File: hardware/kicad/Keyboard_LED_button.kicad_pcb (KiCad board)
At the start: 2 copper layers, 20 x 20 mm, 27 parts, among them J1 JST 4 Pin Qwiic I2C Connector, J2 JST 4 Pin Qwiic I2C Connector, J3 Castellated_Edge_4pin_Qwiic_S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, J4 Castellated_Edge_5pin_Firmware, SW1 SW_Push, U1 CH32V003F4U6, U2 MT3540‑F23

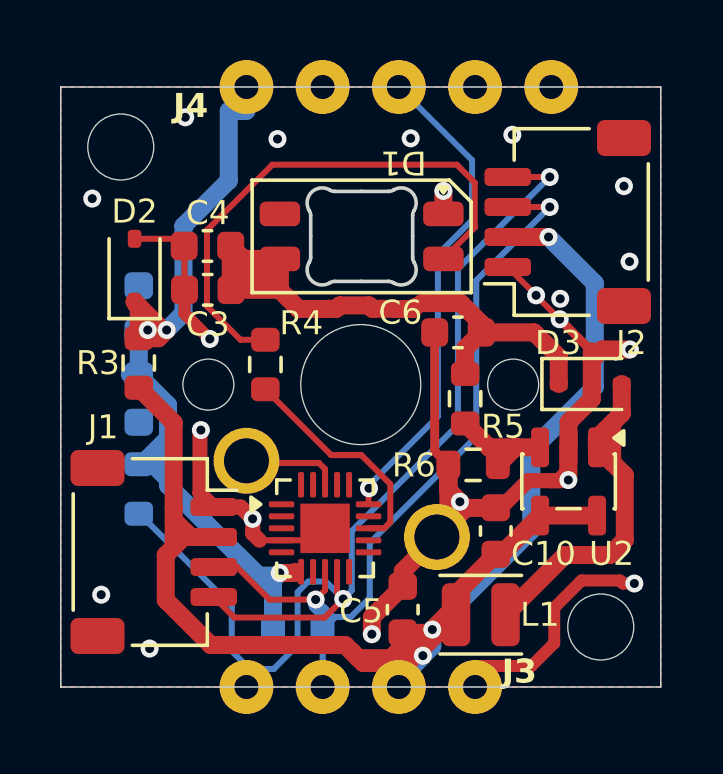
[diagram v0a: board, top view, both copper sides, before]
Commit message: LED Button V2 hardware: updated KiCad schematic + PCB; add V2 + V1.1 schematic PDFs
Updated Keyboard_LED_button KiCad project (schematic + board) for v2.0; added
Schematics_LEDButton_V2_20260616.pdf and renamed-as Schematics_LEDButton_V1_1_20260408.pdf;
removed obsolete Schematics_Keyboard_Button_20260408.pdf and .keep placeholders.
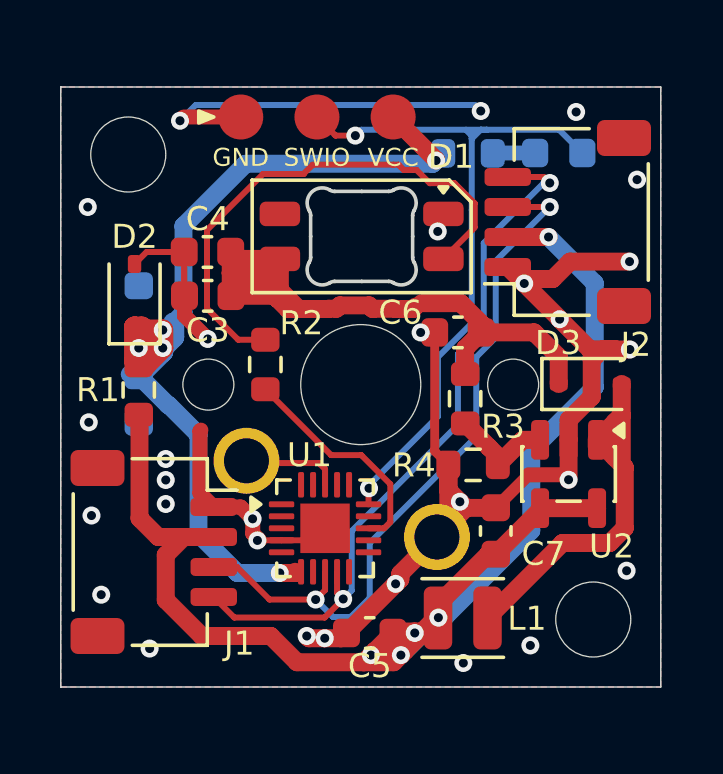
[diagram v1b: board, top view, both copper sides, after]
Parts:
- removed H2: MountingHole, MountingHole:MountingHole_2.2mm_M2
- removed J4: Castellated_Edge_5pin_Firmware, Chris_Library:Castellated_edge_pad_Firmware
- removed the R1 at (122.6, 93.4)
- removed the R2 at (127.9, 98.1)
- added D4: LED, LED_SMD:LED_0603_1608Metric, B.Cu at (136.6, 82.2)
- added R5: 2.2k, Resistor_SMD:R_0603_1608Metric, B.Cu at (133.6, 82.2)
- H1: value MountingHole -> noknok_MountingHole; footprint MountingHole:MountingHole_2.2mm_M2 -> noknok:noknok_MountingHole_2.5mm_M2.5
- J3: value Castellated_Edge_4pin_Qwiic_StemmaQT-I2C -> noknok_FlashPads_I2C-module; footprint Chris_Library:Castellated_edge_pad_I2C_4pin -> noknok:noknok_FlashPads_I2C-module_1x3_M2.5
- moved H1 22.3 mm to (137.8, 97.8)
- moved J3 21.2 mm to (122.2, 82.2), turned to 0 degrees
- moved C5 1.35 mm to (130.3, 98.2), turned to 180 degrees
- moved R1 0.90 mm to (122.6, 90.1)
- moved D2 0.84 mm to (122.5, 87.0)
- moved L1 0.61 mm to (133.4, 97.7)
- moved U2 0.25 mm to (136.9, 92.9)
- moved C4 0.20 mm to (124.9, 85.5)
- moved C3 0.20 mm to (124.9, 87.0)
- renumbered C10 to C7, R3 to R1, R4 to R2, R5 to R3, R6 to R4
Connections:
- J3 pad 2: +3.3V-IN -> Net-(D4-K)
- J3 pad 3: Net-(J1-Pin_3) -> +3.3V-PROT
- U1 pad 15: Net-(J4-SWIO) -> Net-(D4-K)
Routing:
- net Net-(D4-K): track 0.00 -> 25.2 mm, vias 0 -> 2
- net Net-(J4-SWIO): track 16.2 -> 0.00 mm, vias 1 -> 0
- net Net-(J1-Pin_4): track 37.6 -> 24.3 mm
- net GND: track 51.3 -> 60.8 mm, vias 21 -> 29
- net +3.3V-PROT: track 30.7 -> 37.0 mm, vias 3 -> 5
- net +4.3V: track 21.8 -> 24.7 mm
- net Net-(D3-A): track 12.2 -> 14.9 mm
- net Net-(J1-Pin_3): track 26.7 -> 24.5 mm
- net +3.3V-IN: track 53.8 -> 55.8 mm, vias 3 -> 5
- net Net-(D4-A): track 0.00 -> 1.43 mm
- net Net-(U2-FB): track 4.60 -> 3.78 mm
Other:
- board text added: "KB_Button V2_Jun26"
- board text removed: "J3"
- board text removed: "J4"
- board text removed: "KB_Button_V1_Apr26"
